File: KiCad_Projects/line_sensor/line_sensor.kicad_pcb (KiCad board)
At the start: 2 copper layers, 20.3 x 15.2 mm, 4 parts, among them J1 Conn_01x05_Female, U1 S4282-51, U2 S4282-51

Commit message: 基盤データのアップデート
ローカルコミットはちゃんと作ってください
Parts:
- added C1: C_Small, Capacitor_THT:C_Disc_D3.8mm_W2.6mm_P2.50mm, F.Cu at (163.1, 99.1)
- added C10: C_Small, Capacitor_THT:C_Disc_D3.8mm_W2.6mm_P2.50mm, F.Cu at (188.5, 74.1)
- added C11: C_Small, Capacitor_THT:C_Disc_D3.8mm_W2.6mm_P2.50mm, F.Cu at (188.5, 78.3)
- added C12: C_Small, Capacitor_THT:C_Disc_D3.8mm_W2.6mm_P2.50mm, F.Cu at (163.1, 94.9)
- added C13: C_Small, Capacitor_THT:C_Disc_D3.8mm_W2.6mm_P2.50mm, F.Cu at (182.9, 78.3)
- added C14: C_Small, Capacitor_THT:C_Disc_D3.8mm_W2.6mm_P2.50mm, F.Cu at (163.1, 90.8)
- added C15: C_Small, Capacitor_THT:C_Disc_D3.8mm_W2.6mm_P2.50mm, F.Cu at (151.3, 110.0)
- added C16: C_Small, Capacitor_THT:C_Disc_D3.8mm_W2.6mm_P2.50mm, F.Cu at (172.4, 85.2)
- added C2: C_Small, Capacitor_THT:C_Disc_D3.8mm_W2.6mm_P2.50mm, F.Cu at (177.0, 79.7)
- added C3: C_Small, Capacitor_THT:C_Disc_D3.8mm_W2.6mm_P2.50mm, F.Cu at (182.9, 74.1)
- added C4: C_Small, Capacitor_THT:C_Disc_D3.8mm_W2.6mm_P2.50mm, F.Cu at (168.7, 94.9)
- added C5: C_Small, Capacitor_THT:C_Disc_D3.8mm_W2.6mm_P2.50mm, F.Cu at (174.4, 89.4)
- added C6: C_Small, Capacitor_THT:C_Disc_D3.8mm_W2.6mm_P2.50mm, F.Cu at (168.7, 90.8)
- added C7: C_Small, Capacitor_THT:C_Disc_D3.8mm_W2.6mm_P2.50mm, F.Cu at (157.2, 104.5)
- added C8: C_Small, Capacitor_THT:C_Disc_D3.8mm_W2.6mm_P2.50mm, F.Cu at (156.9, 110.0)
- added C9: C_Small, Capacitor_THT:C_Disc_D3.8mm_W2.6mm_P2.50mm, F.Cu at (178.0, 83.8)
- added D10: LED, LED_THT:LED_D3.0mm_Clear, F.Cu at (151.4, 105.2)
- added D11: LED, LED_THT:LED_D3.0mm_Clear, F.Cu at (151.4, 94.1)
- added D12: LED, LED_THT:LED_D3.0mm_Clear, F.Cu at (165.3, 74.8)
- added D13: LED, LED_THT:LED_D3.0mm_Clear, F.Cu at (145.5, 105.2)
- added D14: LED, LED_THT:LED_D3.0mm_Clear, F.Cu at (157.3, 94.1)
- added D15: LED, LED_THT:LED_D3.0mm_Clear, F.Cu at (145.5, 94.1)
- added D16: LED, LED_THT:LED_D3.0mm_Clear, F.Cu at (165.3, 80.4)
- added D2: LED, LED_THT:LED_D3.0mm_Clear, F.Cu at (171.2, 74.8)
- added D3: LED, LED_THT:LED_D3.0mm_Clear, F.Cu at (166.6, 85.9)
- added D4: LED, LED_THT:LED_D3.0mm_Clear, F.Cu at (177.1, 74.8)
- added D5: LED, LED_THT:LED_D3.0mm_Clear, F.Cu at (157.3, 99.6)
- added D6: LED, LED_THT:LED_D3.0mm_Clear, F.Cu at (160.7, 85.9)
- added D7: LED, LED_THT:LED_D3.0mm_Clear, F.Cu at (171.2, 80.4)
- added D8: LED, LED_THT:LED_D3.0mm_Clear, F.Cu at (151.4, 99.6)
- added D9: LED, LED_THT:LED_D3.0mm_Clear, F.Cu at (145.5, 110.7)
- added U10: S4282-51, Line_sennsor:Line_sennsor, F.Cu at (129.4, 72.8)
- added U11: S4282-51, Line_sennsor:Line_sennsor, F.Cu at (132.4, 82.4)
- added U12: S4282-51, Line_sennsor:Line_sennsor, F.Cu at (147.6, 82.4)
- added U13: S4282-51, Line_sennsor:Line_sennsor, F.Cu at (140.0, 92.0)
- added U14: S4282-51, Line_sennsor:Line_sennsor, F.Cu at (132.4, 101.7)
- added U15: S4282-51, Line_sennsor:Line_sennsor, F.Cu at (140.0, 82.4)
- added U16: S4282-51, Line_sennsor:Line_sennsor, F.Cu at (155.2, 82.4)
- added U3: S4282-51, Line_sennsor:Line_sennsor, F.Cu at (152.2, 72.8)
- added U4: S4282-51, Line_sennsor:Line_sennsor, F.Cu at (132.4, 92.0)
- added U5: S4282-51, Line_sennsor:Line_sennsor, F.Cu at (124.8, 94.7)
- added U6: S4282-51, Line_sennsor:Line_sennsor, F.Cu at (144.6, 72.8)
- added U7: S4282-51, Line_sennsor:Line_sennsor, F.Cu at (124.8, 104.3)
- added U8: S4282-51, Line_sennsor:Line_sennsor, F.Cu at (159.8, 72.8)
- added U9: S4282-51, Line_sennsor:Line_sennsor, F.Cu at (140.0, 101.7)
- J1: value Conn_01x05_Female -> Conn_01x04_Female; footprint Connector_PinHeader_2.54mm:PinHeader_1x05_P2.54mm_Vertical -> Connector_PinSocket_2.54mm:PinSocket_1x04_P2.54mm_Vertical
- U1, U2: footprint line_sensor:S4282-51 -> Line_sennsor:Line_sennsor
- moved J1 25.8 mm to (123.3, 74.4)
- moved U1 17.5 mm to (124.8, 85.0), turned to 0 degrees
- moved U2 13.8 mm to (137.0, 72.8), turned to 0 degrees
- moved D1 9.02 mm to (145.5, 99.6), turned to 0 degrees
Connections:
- net Net-(J1-Pad1) renamed 1
- D1 pad 2: Net-(D1-Pad2) -> 5
- J1 pad 4: unconnected-(J1-Pad4) -> 5
- U1 pad 1: Net-(D1-Pad2) -> Net-(D1-Pad1)
- U2 pad 1: Net-(D1-Pad2) -> Net-(D2-Pad1)
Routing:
- net GND: track 16.7 -> 0.00 mm
- net 1: track 13.4 -> 0.00 mm
- net +5V: track 13.2 -> 0.00 mm
- net Net-(D1-Pad2): track 9.45 -> 0.00 mm
- net Net-(D1-Pad1): track 8.89 -> 0.00 mm
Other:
- board outline removed

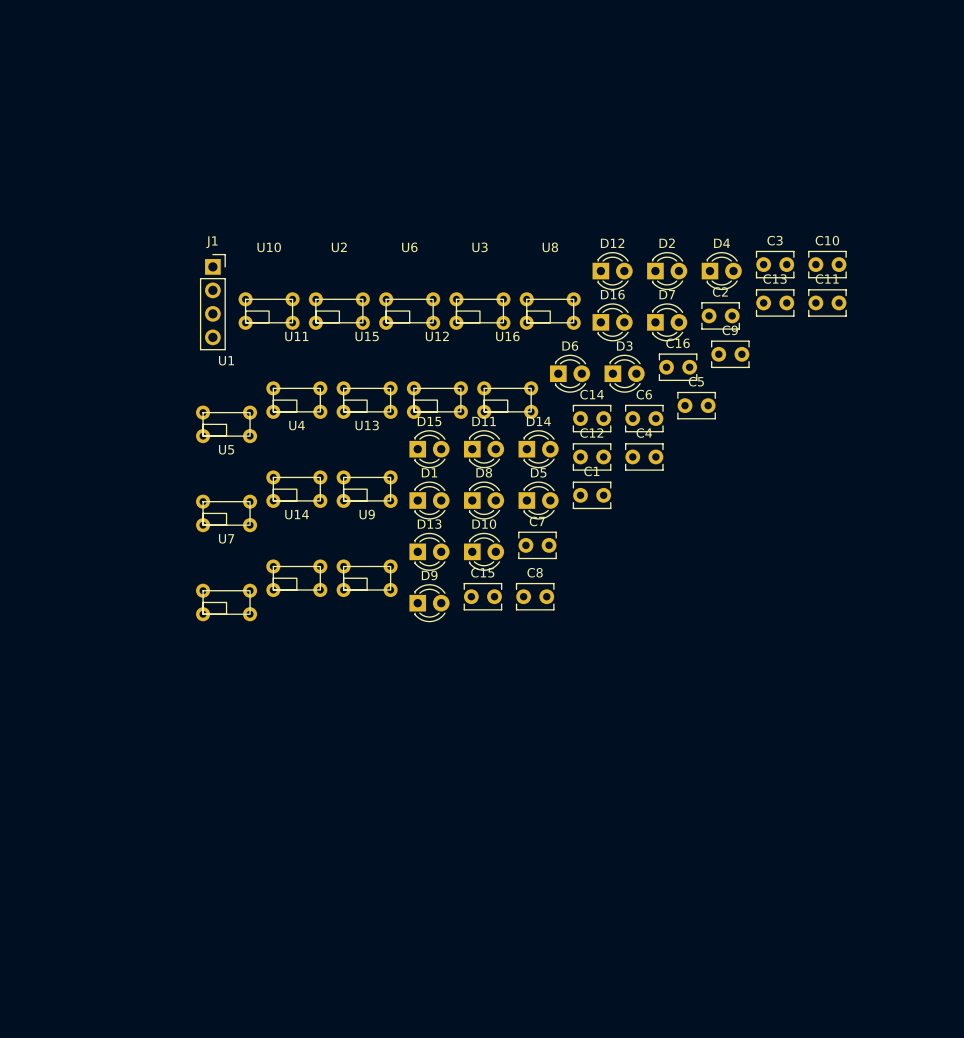
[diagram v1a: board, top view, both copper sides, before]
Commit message: 基板データの更新
ラインセンサーの完成
Arduino メイン基板の作成、製作開始。
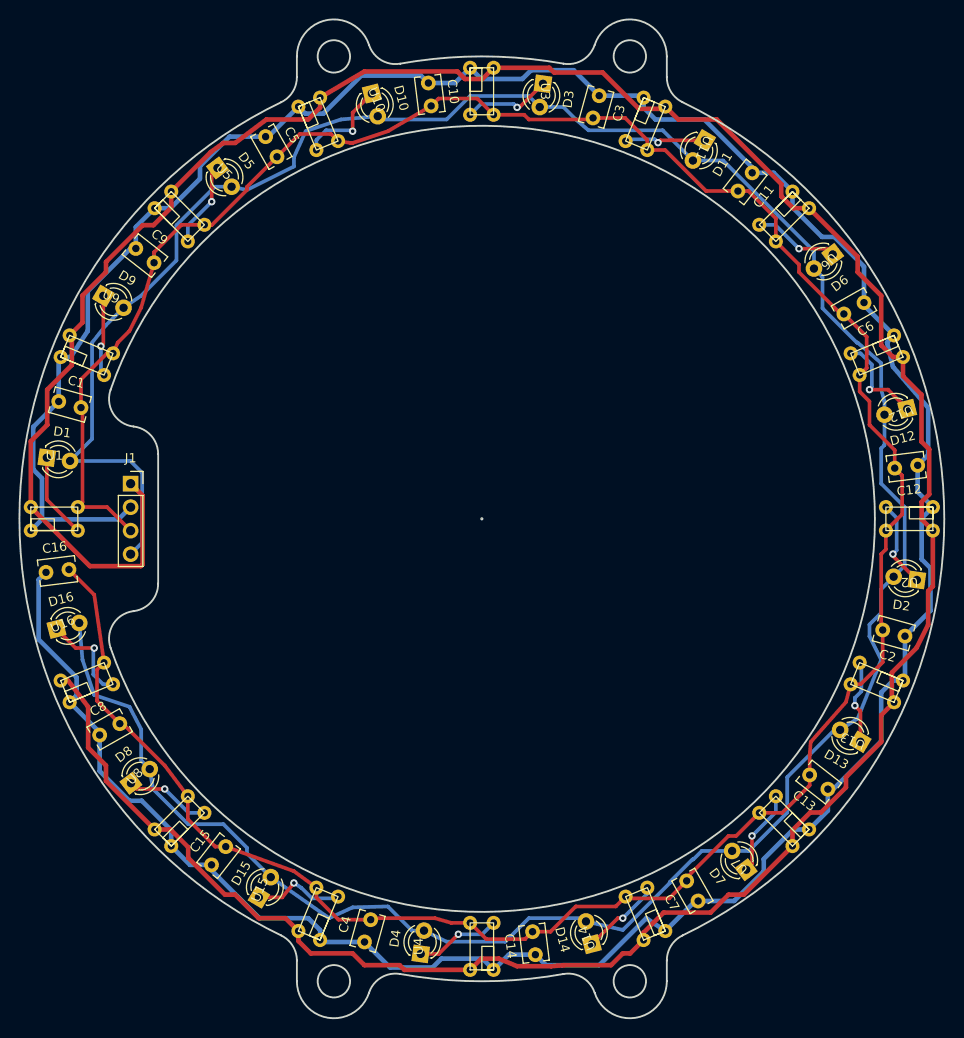
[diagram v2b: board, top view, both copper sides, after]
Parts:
- moved D4 80.2 mm to (145.8, 148.6), turned to 82 degrees
- moved U8 72.4 mm to (115.2, 129.8), turned to 45 degrees
- moved U2 71.0 mm to (198.6, 108.0), turned to 180 degrees
- moved C16 70.7 mm to (105.3, 107.4), turned to 7 degrees
- moved D16 67.5 mm to (106.4, 113.5), turned to 14.5 degrees
- moved U7 65.6 mm to (180.6, 138.8), turned to 135 degrees
- moved C9 64.1 mm to (115.0, 72.4), turned to -38 degrees
- moved U13 62.2 mm to (192.7, 125.2), turned to 157.5 degrees
- moved U15 60.5 mm to (128.8, 141.9), turned to 67.5 degrees
- moved D7 60.0 mm to (181.0, 139.5), turned to 127 degrees
- moved C4 59.9 mm to (139.7, 147.4), turned to 74.5 degrees
- moved C14 58.2 mm to (158.2, 148.7), turned to 97 degrees
- moved U4 57.4 mm to (146.1, 147.8), turned to 90 degrees
- moved C1 57.3 mm to (106.6, 88.9), turned to -15.5 degrees
- moved U16 57.1 mm to (107.3, 113.4), turned to 22.5 degrees
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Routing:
- net GND: track 0.00 -> 343.9 mm
- net 1: track 0.00 -> 334.2 mm
- net 5: track 0.00 -> 305.8 mm
- net +5V: track 0.00 -> 302.0 mm
- net Net-(D12-Pad1): track 0.00 -> 10.5 mm, vias 0 -> 1
- net Net-(D10-Pad1): track 0.00 -> 10.4 mm, vias 0 -> 1
- net Net-(D16-Pad1): track 0.00 -> 10.4 mm, vias 0 -> 1
- net Net-(D15-Pad1): track 0.00 -> 10.0 mm, vias 0 -> 1
- net Net-(D2-Pad1): track 0.00 -> 9.60 mm, vias 0 -> 1
- net Net-(D3-Pad1): track 0.00 -> 9.57 mm, vias 0 -> 1
- net Net-(D1-Pad1): track 0.00 -> 9.27 mm
- net Net-(D4-Pad1): track 0.00 -> 9.27 mm, vias 0 -> 1
- net Net-(D5-Pad1): track 0.00 -> 9.27 mm, vias 0 -> 1
- net Net-(D8-Pad1): track 0.00 -> 9.27 mm, vias 0 -> 1
- net Net-(D6-Pad1): track 0.00 -> 9.27 mm, vias 0 -> 1
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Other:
- board outline added: 100 x 108 mm

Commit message: 基板データの更新
IO基板、ライン基板、電源基盤のコネクタ変更、最終確認
メイン基板制作中。
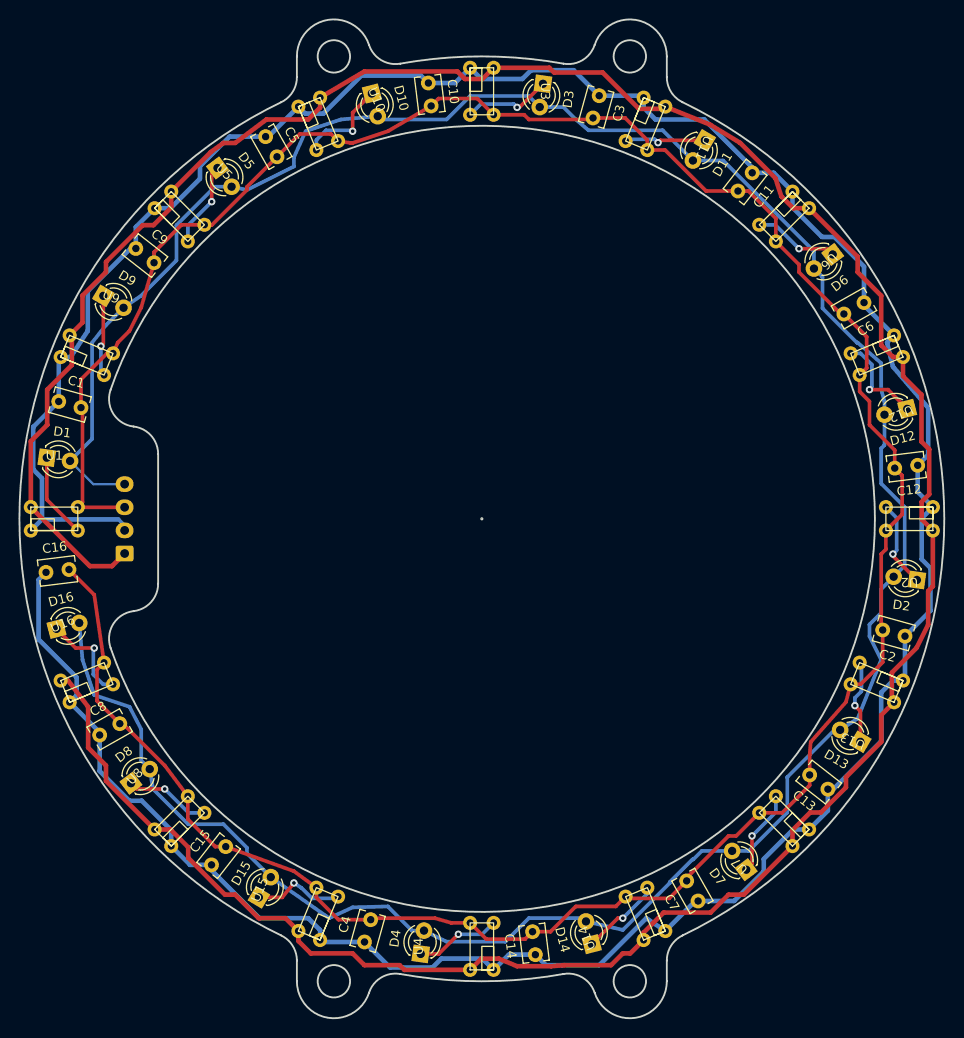
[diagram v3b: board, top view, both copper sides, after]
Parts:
- J1: footprint Connector_PinSocket_2.54mm:PinSocket_1x04_P2.54mm_Vertical -> Connector_JST:JST_XH_B4B-XH-A_1x04_P2.50mm_Vertical; moved to B.Cu
- moved J1 7.58 mm to (113.8, 105.3), turned to 90 degrees
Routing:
- net 1: track 334.2 -> 322.6 mm
- net 5: track 305.8 -> 295.1 mm
- net +5V: track 302.0 -> 300.3 mm

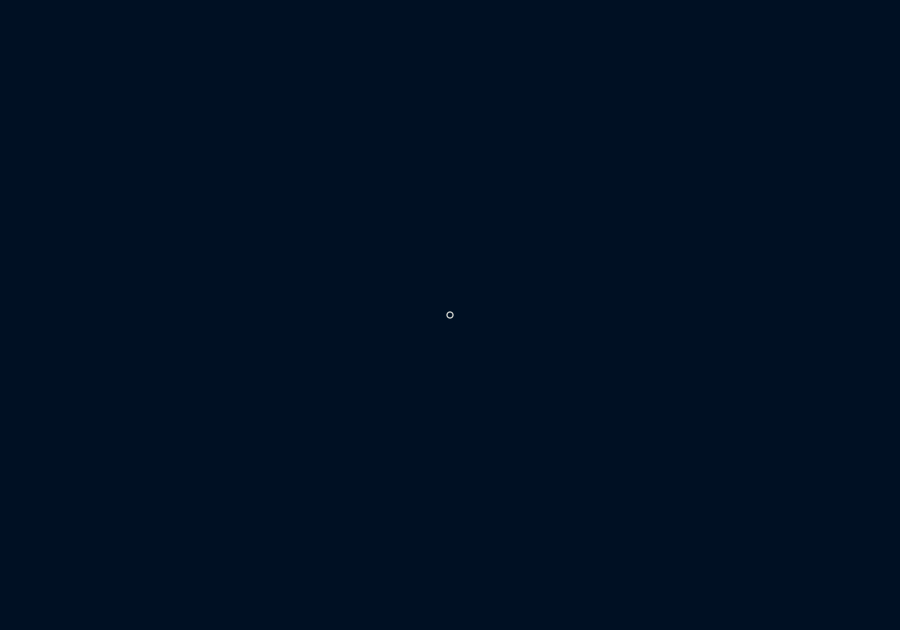
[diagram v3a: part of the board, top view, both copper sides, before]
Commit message: 基板データの更新
メイン基板の部品配置まででけた
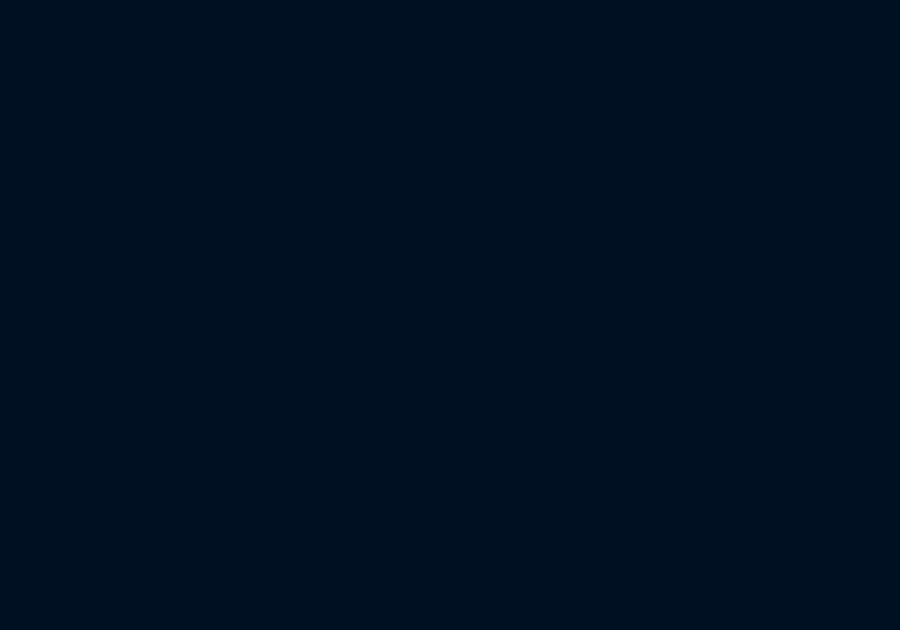
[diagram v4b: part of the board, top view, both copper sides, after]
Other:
- outline, holes or cut-outs redrawn
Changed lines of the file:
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@@
   (gr_line (start 172.4 53.850654) (end 172.4 51.6) (layer "Edge.Cuts") (width 0.2))
   (gr_arc (start 140.203005 152.839819) (mid 141.514899 151.19533) (end 143.584207 150.816682) (layer "Edge.Cuts") (width 0.2))
-  (gr_circle (center 152.4 101.6) (end 152.5 101.6) (layer "Edge.Cuts") (width 0.0001) (fill solid))
   (gr_arc (start 174.098113 56.553448) (mid 202.4 101.6) (end 174.098113 146.646552) (layer "Edge.Cuts") (width 0.2))
   (gr_arc (start 132.4 53.850655) (mid 131.940242 55.44664) (end 130.701887 56.553448) (layer "Edge.Cuts") (width 0.2))

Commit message: 基板データの更新
最後に更新してからのデータ全てです。
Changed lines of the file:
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@@
     (aux_axis_origin 152.4 101.6)
     (pcbplotparams
-      (layerselection 0x0001000_fffffffe)
+      (layerselection 0x00010f0_ffffffff)
       (disableapertmacros false)
       (usegerberextensions false)
-      (usegerberattributes true)
-      (usegerberadvancedattributes true)
+      (usegerberattributes false)
+      (usegerberadvancedattributes false)
       (creategerberjobfile false)
       (svguseinch false)
@@
     (fp_line (start -2.45 -3.4) (end 9.95 -3.4) (layer "B.Fab") (width 0.1))
     (fp_line (start 9.95 -3.4) (end 9.95 2.35) (layer "B.Fab") (width 0.1))
-    (pad "1" thru_hole roundrect (at 0 0 90) (size 1.7 1.95) (drill 0.95) (layers *.Cu *.Mask) (roundrect_rratio 0.147059)
+    (pad "1" thru_hole roundrect (at 0 0 90) (size 1.7 1.95) (drill 0.95) (layers *.Cu *.Mask) (roundrect_rratio 0.1470588235)
       (net 20 "1") (pinfunction "Pin_1") (pintype "passive"))
     (pad "2" thru_hole oval (at 2.5 0 90) (size 1.7 1.95) (drill 0.95) (layers *.Cu *.Mask)
